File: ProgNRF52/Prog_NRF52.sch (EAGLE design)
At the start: 44 parts, among them J3 MEC1-108-02-XX-D-A, U1 TS5A9411, U2 SN74LVC1GU04DBV, U3 TS5A9411, U4 TS5A9411, U5 SN74LVC1GU04DBV, U6 TXB0102D

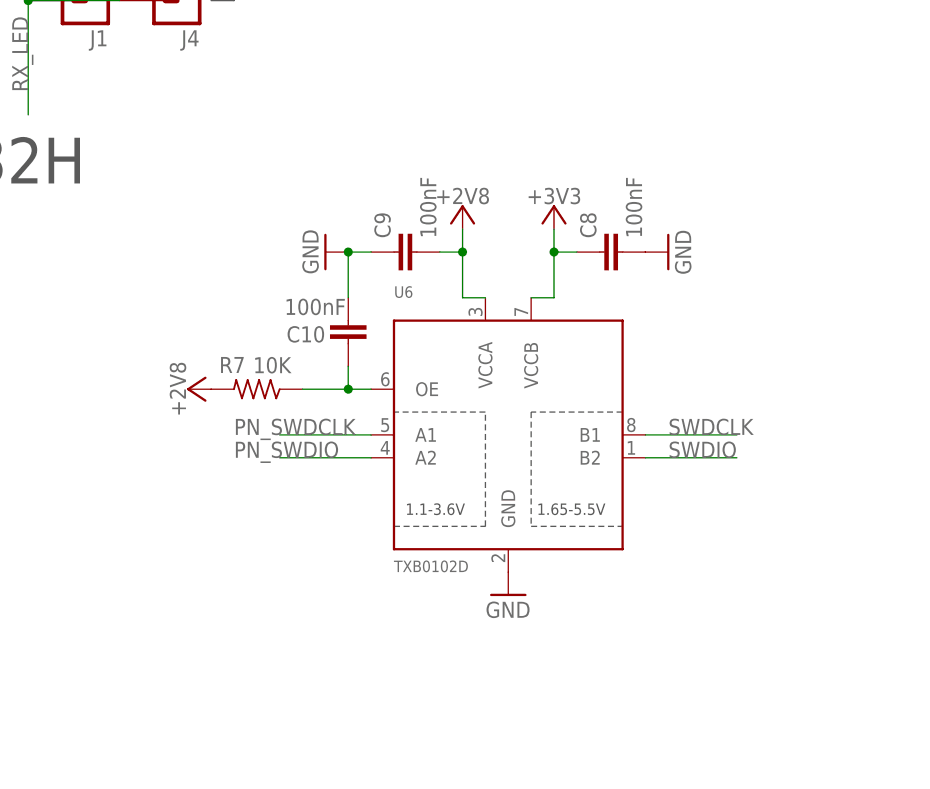
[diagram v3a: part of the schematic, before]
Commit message: Test : remove voltage translation unit
Remove to test revory sch
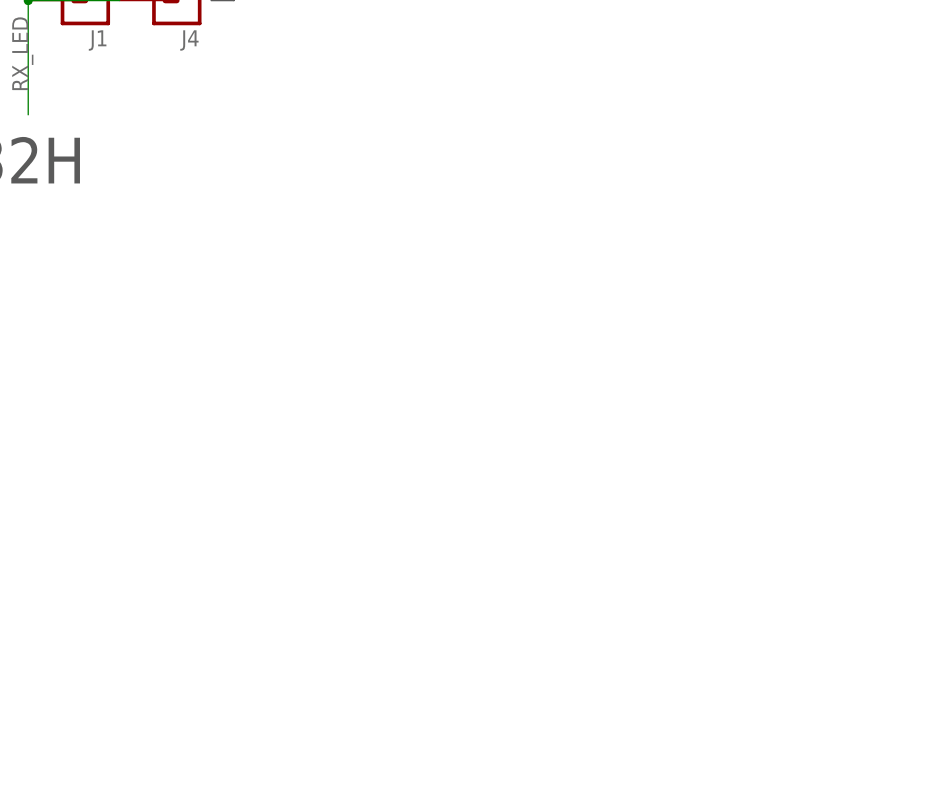
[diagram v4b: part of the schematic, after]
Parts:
- removed C10, C8, C9: 100nF, rcl:C-EUC0603K
- removed R7: 10K, resistor:R-US_R0603
- removed U6: TXB0102D, Tmp_PN:TXB0102D
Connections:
- removed net N$27: C10.1, R7.1, U6.OE
- net +2V8: no longer C9.2, R7.2, U6.VCCA
- net +3V3: no longer C8.1, U6.VCCB
- net GND: no longer C10.2, C8.2, C9.1, U6.GND
- net PN_SWDCLK: no longer U6.A1
- net PN_SWDIO: no longer U6.A2
- net SWDCLK: no longer U6.B1
- net SWDIO: no longer U6.B2
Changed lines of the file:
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@@
 <part name="P+3" library="supply1" deviceset="+5V" device=""/>
 <part name="GND16" library="supply1" deviceset="GND" device=""/>
-<part name="U6" library="Tmp_PN" deviceset="TXB0102D" device=""/>
 <part name="U7" library="Tmp_PN" deviceset="NCP114ASN280T1G" device=""/>
 <part name="TP1" library="testpad" deviceset="TP" device="PAD1-13" value="TPPAD1-13"/>
@@
 <part name="GND18" library="supply1" deviceset="GND" device=""/>
 <part name="GND19" library="supply1" deviceset="GND" device=""/>
-<part name="U$3" library="supply1" deviceset="+2V8" device=""/>
-<part name="V11" library="supply1" deviceset="+3V3" device=""/>
-<part name="GND20" library="supply1" deviceset="GND" device=""/>
-<part name="C8" library="rcl" deviceset="C-EU" device="C0603K" value="100nF"/>
-<part name="C9" library="rcl" deviceset="C-EU" device="C0603K" value="100nF"/>
-<part name="GND21" library="supply1" deviceset="GND" device=""/>
-<part name="GND22" library="supply1" deviceset="GND" device=""/>
-<part name="C10" library="rcl" deviceset="C-EU" device="C0603K" value="100nF"/>
-<part name="R7" library="resistor" deviceset="R-US_" device="R0603" value="10K"/>
-<part name="U$4" library="supply1" deviceset="+2V8" device=""/>
 <part name="GND23" library="supply1" deviceset="GND" device=""/>
 <part name="R9" library="resistor" deviceset="R-US_" device="R0603" value="NC"/>
@@
 <instance part="P+3" gate="1" x="104.14" y="236.22"/>
 <instance part="GND16" gate="1" x="127" y="236.22" rot="R180"/>
-<instance part="U6" gate="G$1" x="215.9" y="91.44"/>
 <instance part="U7" gate="G$1" x="210.82" y="40.64"/>
 <instance part="TP1" gate="G$1" x="246.38" y="228.6" rot="R90"/>
@@
 <instance part="GND18" gate="1" x="210.82" y="25.4"/>
 <instance part="GND19" gate="1" x="233.68" y="30.48"/>
-<instance part="U$3" gate="G$1" x="210.82" y="119.38"/>
-<instance part="V11" gate="G$1" x="220.98" y="119.38"/>
-<instance part="GND20" gate="1" x="215.9" y="76.2"/>
-<instance part="C8" gate="G$1" x="226.06" y="114.3" rot="R90"/>
-<instance part="C9" gate="G$1" x="203.2" y="114.3" rot="R90"/>
-<instance part="GND21" gate="1" x="233.68" y="114.3" rot="R90"/>
-<instance part="GND22" gate="1" x="195.58" y="114.3" rot="R270"/>
-<instance part="C10" gate="G$1" x="198.12" y="104.14" smashed="yes" rot="R180">
-<attribute name="NAME" x="195.58" y="106.045" size="1.778" layer="95" rot="R180"/>
-<attribute name="VALUE" x="197.866" y="109.093" size="1.778" layer="96" rot="R180"/>
-</instance>
-<instance part="R7" gate="G$1" x="187.96" y="99.06" smashed="yes" rot="R180">
-<attribute name="NAME" x="186.69" y="102.6414" size="1.778" layer="95" rot="R180"/>
-<attribute name="VALUE" x="191.77" y="102.616" size="1.778" layer="96" rot="R180"/>
-</instance>
-<instance part="U$4" gate="G$1" x="180.34" y="99.06" rot="R90"/>
 <instance part="GND23" gate="1" x="251.46" y="208.28"/>
 <instance part="R9" gate="G$1" x="109.22" y="55.88" rot="R180"/>
@@
 </segment>
 <segment>
-<pinref part="U6" gate="G$1" pin="GND"/>
-<pinref part="GND20" gate="1" pin="GND"/>
-</segment>
-<segment>
-<pinref part="C8" gate="G$1" pin="2"/>
-<pinref part="GND21" gate="1" pin="GND"/>
-</segment>
-<segment>
-<pinref part="C9" gate="G$1" pin="1"/>
-<pinref part="GND22" gate="1" pin="GND"/>
-<wire x1="198.12" y1="114.3" x2="200.66" y2="114.3" width="0.1524" layer="91"/>
-<pinref part="C10" gate="G$1" pin="2"/>
-<wire x1="198.12" y1="109.22" x2="198.12" y2="114.3" width="0.1524" layer="91"/>
-<junction x="198.12" y="114.3"/>
-</segment>
-<segment>
 <pinref part="TP4" gate="G$1" pin="TP"/>
 <pinref part="GND23" gate="1" pin="GND"/>
@@
 <pinref part="C6" gate="G$1" pin="2"/>
 <wire x1="187.96" y1="43.18" x2="193.04" y2="43.18" width="0.1524" layer="91"/>
-</segment>
-<segment>
-<pinref part="U6" gate="G$1" pin="VCCB"/>
-<wire x1="218.44" y1="109.22" x2="220.98" y2="109.22" width="0.1524" layer="91"/>
-<pinref part="V11" gate="G$1" pin="+3V3"/>
-<wire x1="220.98" y1="109.22" x2="220.98" y2="114.3" width="0.1524" layer="91"/>
-<pinref part="C8" gate="G$1" pin="1"/>
-<wire x1="220.98" y1="114.3" x2="220.98" y2="116.84" width="0.1524" layer="91"/>
-<wire x1="223.52" y1="114.3" x2="220.98" y2="114.3" width="0.1524" layer="91"/>
-<junction x="220.98" y="114.3"/>
 </segment>
 </net>
@@
 </segment>
 <segment>
-<pinref part="U6" gate="G$1" pin="A1"/>
-<wire x1="200.66" y1="93.98" x2="190.5" y2="93.98" width="0.1524" layer="91"/>
-<label x="185.42" y="93.98" size="1.778" layer="95"/>
-</segment>
-<segment>
 <pinref part="TP2" gate="G$1" pin="TP"/>
 <wire x1="248.92" y1="223.52" x2="261.62" y2="223.52" width="0.1524" layer="91"/>
@@
 <wire x1="284.48" y1="86.36" x2="274.32" y2="86.36" width="0.1524" layer="91"/>
 <label x="271.78" y="86.36" size="1.778" layer="95"/>
-</segment>
-<segment>
-<pinref part="U6" gate="G$1" pin="B2"/>
-<wire x1="231.14" y1="91.44" x2="241.3" y2="91.44" width="0.1524" layer="91"/>
-<label x="233.68" y="91.44" size="1.778" layer="95"/>
 </segment>
 <segment>
@@
 <junction x="228.6" y="48.26"/>
 </segment>
-<segment>
-<pinref part="U$3" gate="G$1" pin="+2V8"/>
-<wire x1="210.82" y1="116.84" x2="210.82" y2="114.3" width="0.1524" layer="91"/>
-<pinref part="U6" gate="G$1" pin="VCCA"/>
-<wire x1="210.82" y1="114.3" x2="210.82" y2="109.22" width="0.1524" layer="91"/>
-<wire x1="210.82" y1="109.22" x2="213.36" y2="109.22" width="0.1524" layer="91"/>
-<pinref part="C9" gate="G$1" pin="2"/>
-<wire x1="208.28" y1="114.3" x2="210.82" y2="114.3" width="0.1524" layer="91"/>
-<junction x="210.82" y="114.3"/>
-</segment>
-<segment>
-<pinref part="R7" gate="G$1" pin="2"/>
-<pinref part="U$4" gate="G$1" pin="+2V8"/>
-</segment>
 </net>
 <net name="SWDCLK" class="0">
@@
 </segment>
 <segment>
-<pinref part="U6" gate="G$1" pin="B1"/>
-<wire x1="241.3" y1="93.98" x2="231.14" y2="93.98" width="0.1524" layer="91"/>
-<label x="233.68" y="93.98" size="1.778" layer="95"/>
-</segment>
-<segment>
 <pinref part="R9" gate="G$1" pin="1"/>
 <wire x1="114.3" y1="55.88" x2="127" y2="55.88" width="0.1524" layer="91"/>
@@
 <net name="PN_SWDIO" class="0">
 <segment>
-<pinref part="U6" gate="G$1" pin="A2"/>
-<wire x1="200.66" y1="91.44" x2="190.5" y2="91.44" width="0.1524" layer="91"/>
-<label x="185.42" y="91.44" size="1.778" layer="95"/>
-</segment>
-<segment>
 <pinref part="CONN1" gate="G$1" pin="2"/>
 <wire x1="193.04" y1="223.52" x2="200.66" y2="223.52" width="0.1524" layer="91"/>
@@
 </segment>
 </net>
-<net name="N$27" class="0">
-<segment>
-<pinref part="R7" gate="G$1" pin="1"/>
-<pinref part="U6" gate="G$1" pin="OE"/>
-<wire x1="193.04" y1="99.06" x2="198.12" y2="99.06" width="0.1524" layer="91"/>
-<pinref part="C10" gate="G$1" pin="1"/>
-<wire x1="198.12" y1="99.06" x2="200.66" y2="99.06" width="0.1524" layer="91"/>
-<wire x1="198.12" y1="101.6" x2="198.12" y2="99.06" width="0.1524" layer="91"/>
-<junction x="198.12" y="99.06"/>
-</segment>
-</net>

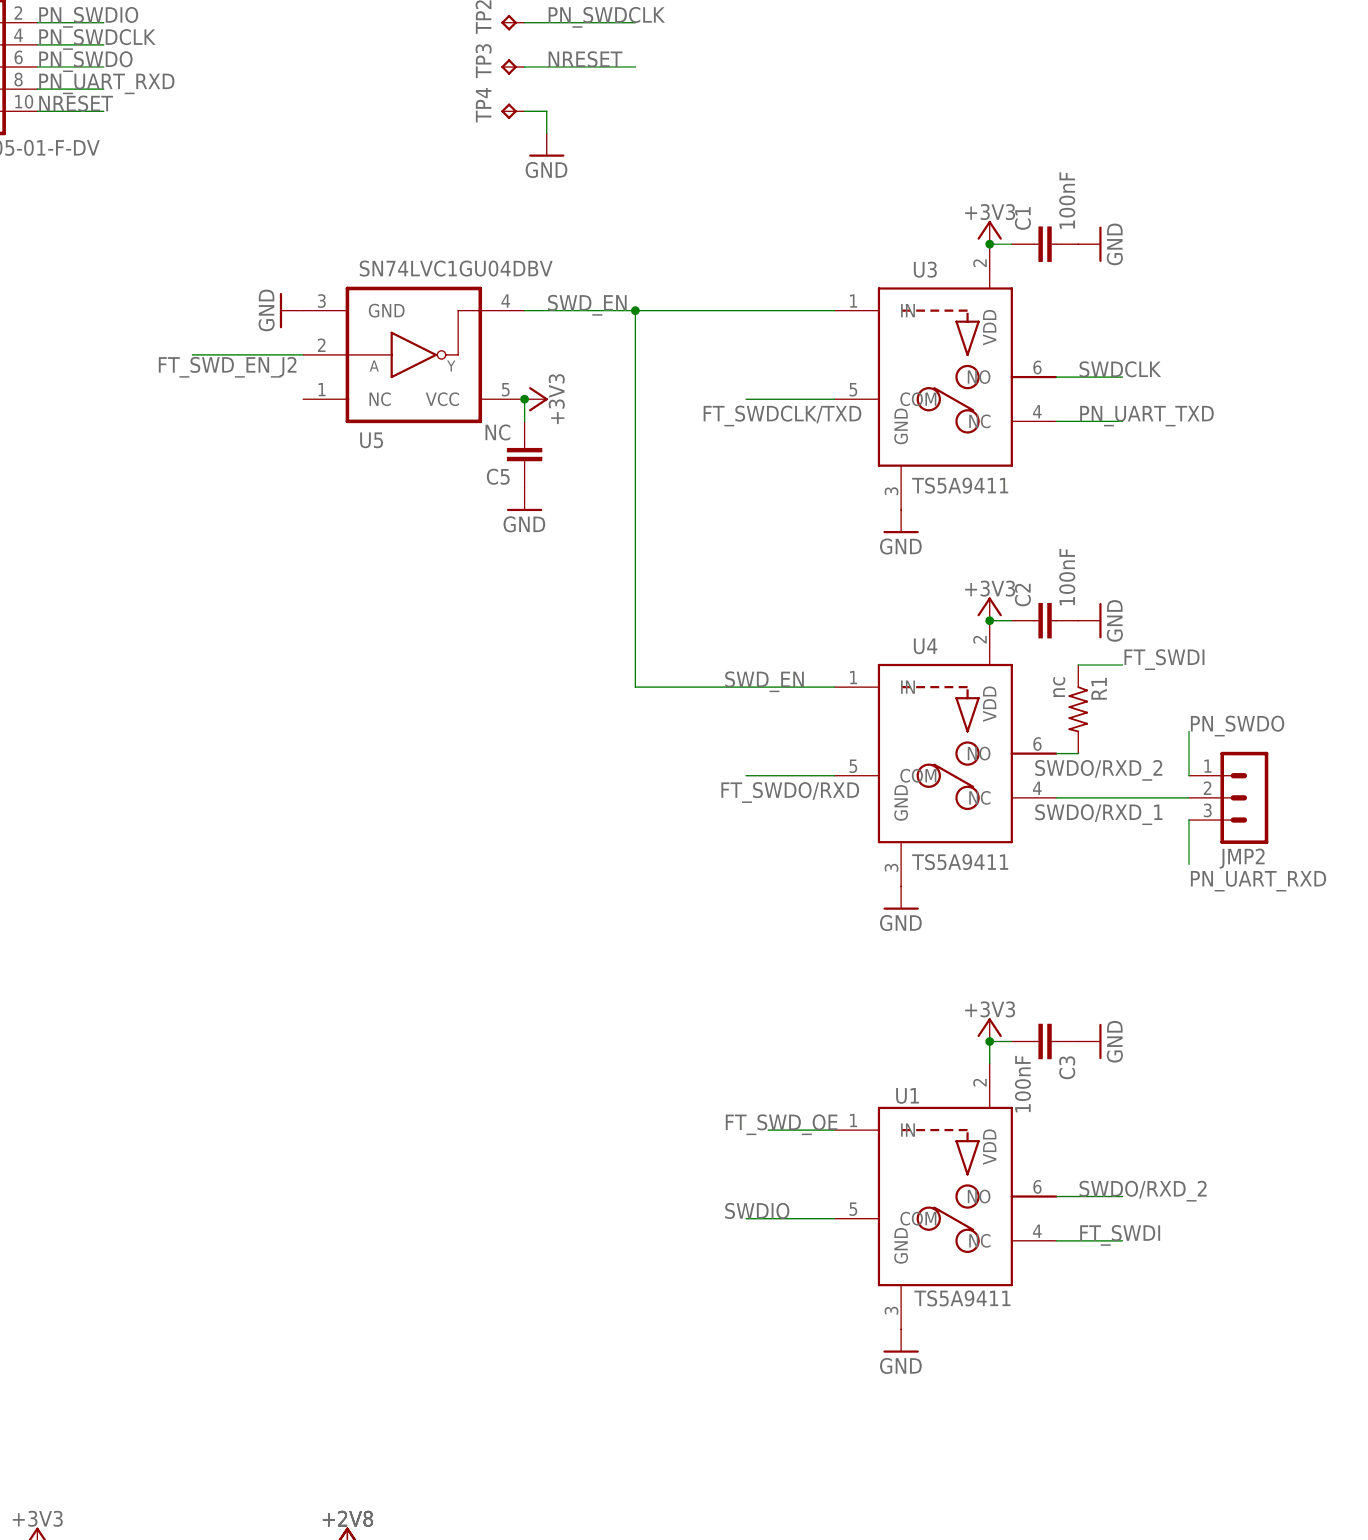
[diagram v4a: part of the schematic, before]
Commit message: Wrong suppressing of logical gates
Consider an error
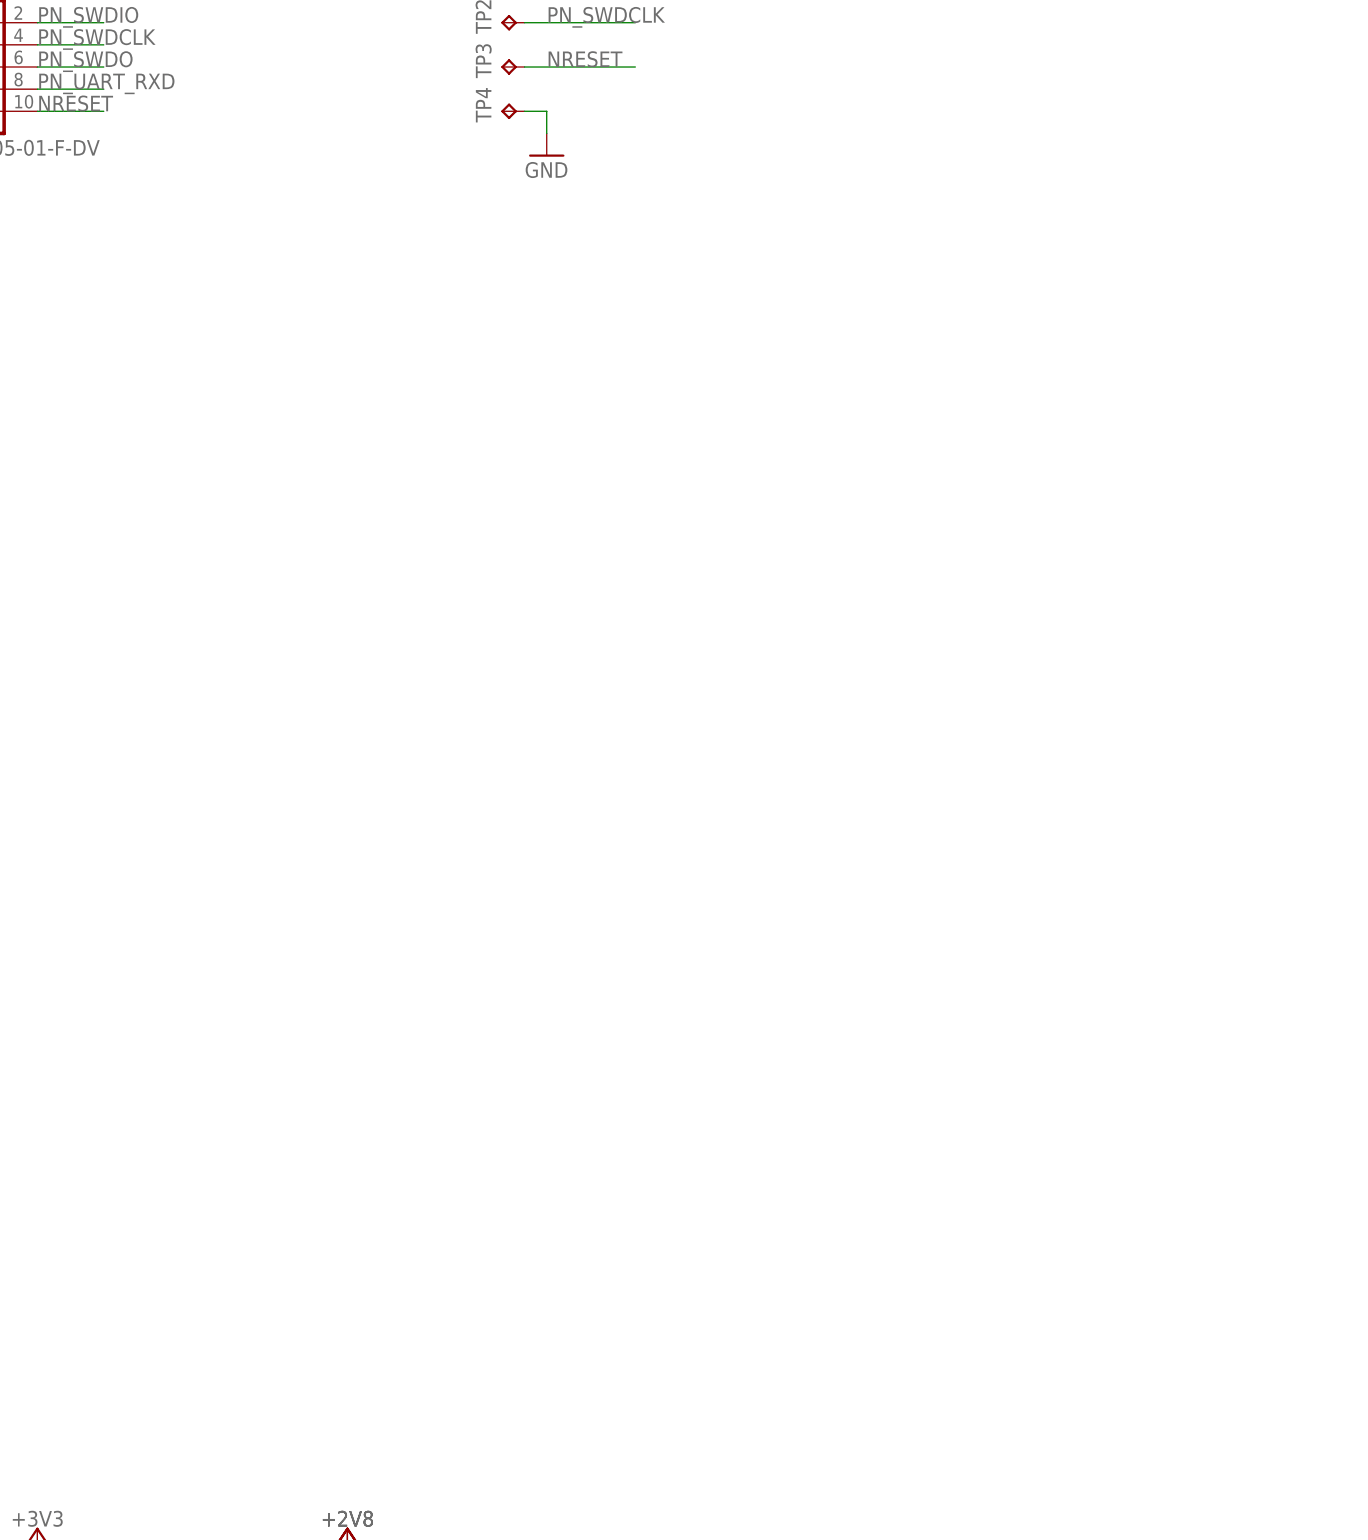
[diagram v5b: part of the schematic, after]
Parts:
- removed C1, C2, C3: 100nF, rcl:C-EUC0603K
- removed C5: NC, rcl:C-EUC0603K
- removed JMP2: (no value), con-lstb:MA03-1
- removed R1: nc, resistor:R-US_R0603
- removed U1, U3, U4: TS5A9411, FabLib:TS5A9411
- removed U5: SN74LVC1GU04DBV, 74LV:SN74LVC1GU04DBV
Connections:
- removed net SWDO/RXD_1: JMP2.2, U4.NC
- removed net SWDO/RXD_2: R1.2, U1.NO, U4.NO
- removed net SWD_EN: U3.IN, U4.IN, U5.Y
- net +3V3: no longer C1.1, C2.1, C3.2, C5.2, U1.VDD, U3.VDD, U4.VDD, U5.VCC
- net FT_SWDCLK/TXD: no longer U3.COM
- net FT_SWDI: no longer R1.1, U1.NC
- net FT_SWDO/RXD: no longer U4.COM
- net FT_SWD_EN_J2: no longer U5.A
- net FT_SWD_OE: no longer U1.IN
- net GND: no longer C1.2, C2.2, C3.1, C5.1, U1.GND, U3.GND, U4.GND, U5.GND
- net PN_SWDO: no longer JMP2.1
- net PN_UART_RXD: no longer JMP2.3
- net PN_UART_TXD: no longer U3.NC
- net SWDCLK: no longer U3.NO
- net SWDIO: no longer U1.COM
